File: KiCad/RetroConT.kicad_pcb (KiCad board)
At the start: 2 copper layers, 200 x 200 mm, 213 parts, among them IC1 BH7236, IC2 EPM7128-J84SOC-RetroCon-eagle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, IC21 4464, IC22 4464, IC23 4464, IC24 4464, IC30 74HC157, IC31 74HC157, IC32 74LS07, IC33 74HC14, IC4 74LVC245, IC6 74HC74, IC7 74HC30, J1 POWER, J10 DIN8_SEL2, J11 DIN8_SEL4, J12 RGB, J14 DIN8_SEL1, J17 USB_A_DUAL, J2 SVideo, J4 DIN8_SEL3, J5 MONO, J7 POWER-OUT, J8 DIN8_SEL5, Q2 21M47727, Q4 TP0606N3, Q5 TP0606N3, SW1 SW_SPDT, SW2 SW_SPDT, SW3 SW_DPDT, U1 LM358, U10 RP5C01A, U11 74LS175, U2 Z80/Z84C00, U3 29x010/20/40, U4 AS6C4008, U5 PUD-0512, U6 MDD02L-12, U7 tinyFPGA, U8 LM1117-33, X1 PS/2 KBD, X2 RAUDIO, X3 JOYSTICK1, X4 JOYSTICK2, X5 LAUDIO, X9 COMPOSITE, Y1 32.768KHz

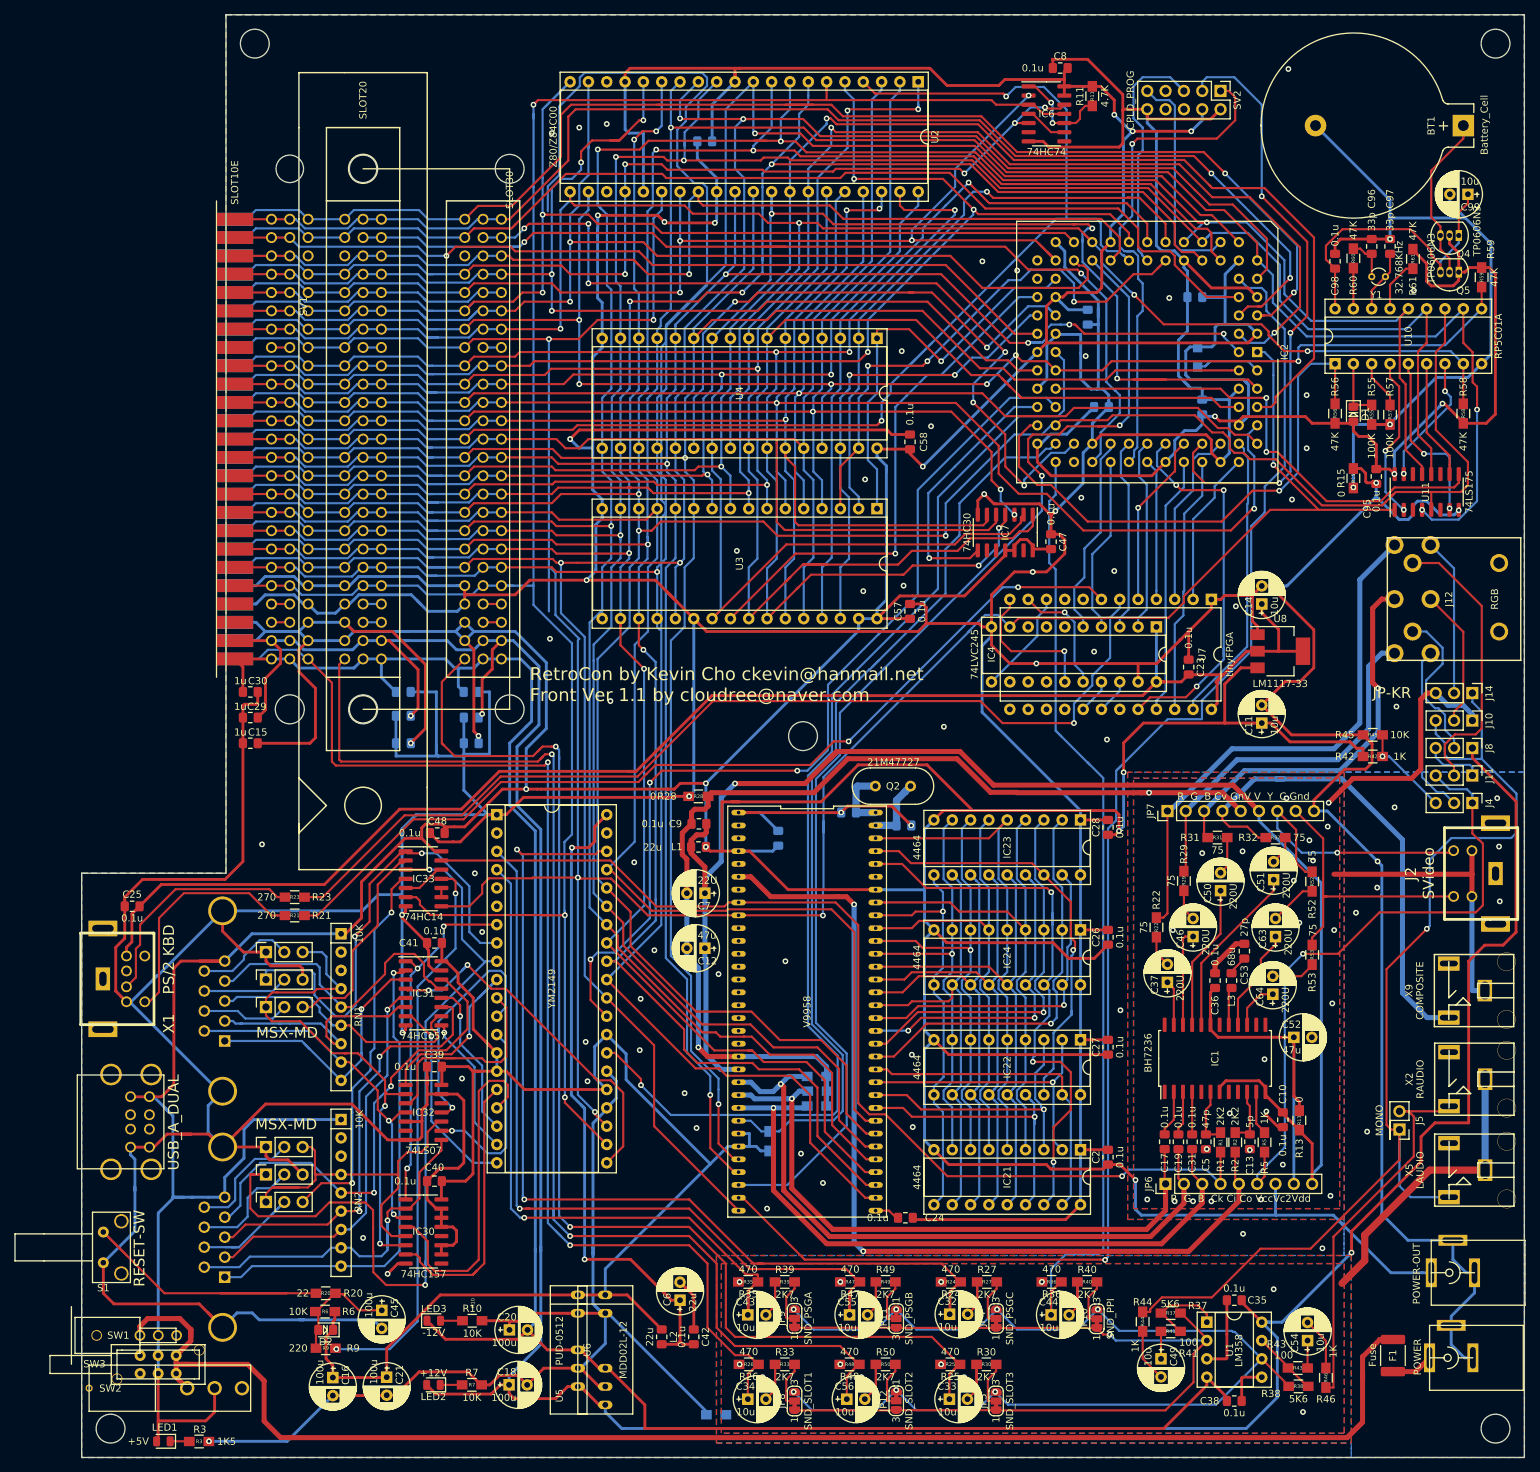
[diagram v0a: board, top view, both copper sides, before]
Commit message: Fix up some bugs
fix up around XTAL and add variable capacitor.
fix the position of Joystick ports.
fix +5V supply around DC2DC.
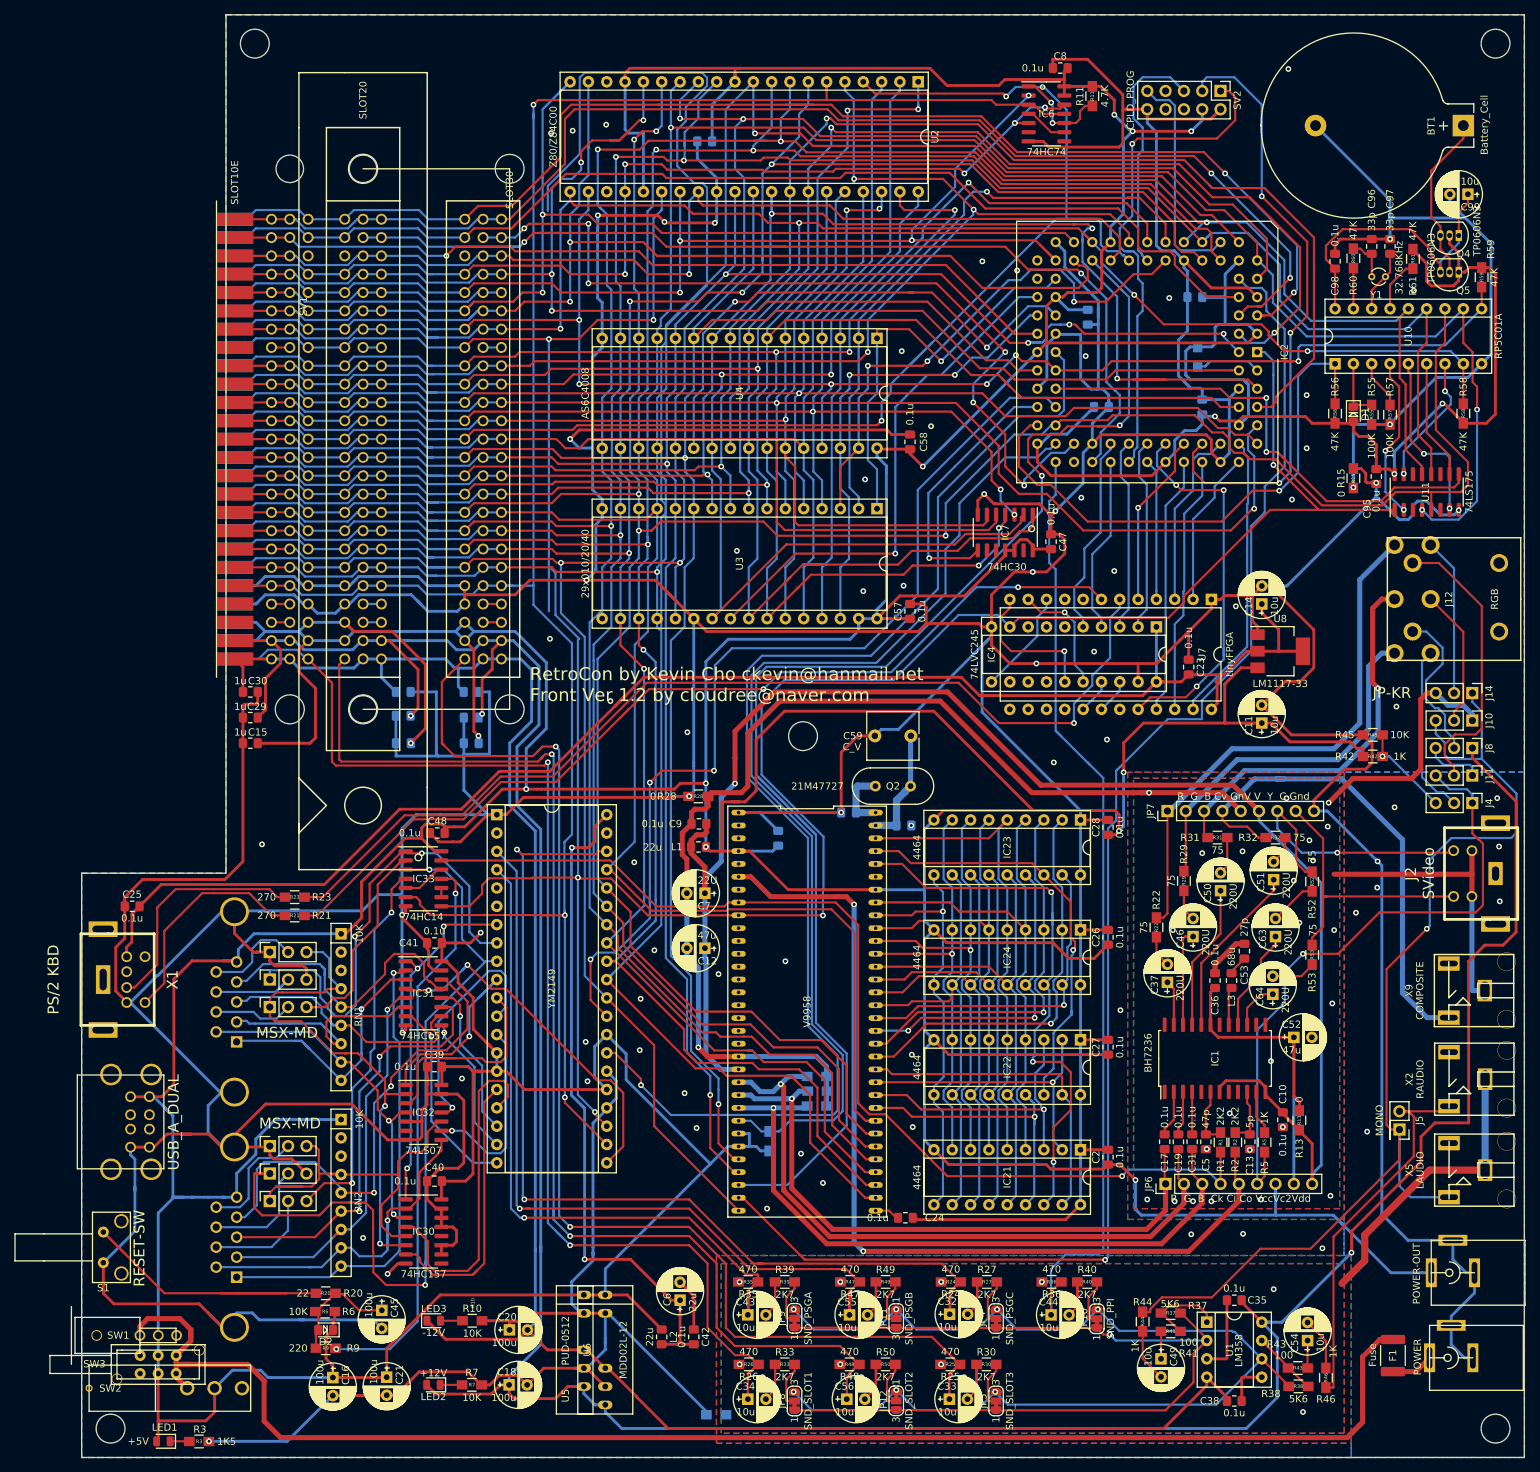
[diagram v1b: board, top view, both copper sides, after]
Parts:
- added C59: C_V, Capacitor_THT:C_Rect_L7.0mm_W6.5mm_P5.00mm, F.Cu at (135.0, 125.0)
- moved X3 1.66 mm to (46.5, 167.4)
- moved X4 1.65 mm to (46.5, 200.0)
- moved U5 0.84 mm to (94.6, 210.1)
- moved JS21 0.55 mm to (51.1, 181.8)
- moved JS22 0.55 mm to (51.1, 185.6)
- moved JS23 0.55 mm to (51.1, 189.5)
- moved JS11 0.53 mm to (51.1, 154.9)
- moved JS12 0.53 mm to (51.1, 158.8)
- moved JS13 0.53 mm to (51.1, 162.6)
- moved X1 0.10 mm to (30.0, 158.8)
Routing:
- net +5V: track 1464.7 -> 1516.2 mm, vias 15 -> 16
- net #VDP_CSW: track 173.1 -> 199.3 mm
- net GND: track 1625.5 -> 1647.5 mm
- net #ExRESET: track 400.1 -> 416.7 mm
- net PSGBDIR: track 161.5 -> 177.4 mm
- net #VDP_INT: track 131.4 -> 143.5 mm
- net VDD_DAC: track 217.7 -> 225.2 mm
- net GNDV: track 234.0 -> 241.5 mm, vias 26 -> 25
- net XTAL1: track 9.16 -> 16.1 mm
- net Q2P7: track 18.7 -> 15.0 mm
- net +3V3: track 208.3 -> 211.7 mm
- net PSGBC1: track 131.4 -> 134.6 mm
- net -12V: track 278.7 -> 276.3 mm
- net J1DN: track 35.6 -> 33.5 mm
- net PSDATA: track 139.0 -> 141.1 mm
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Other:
- board text added: "RetroCon by Kevin Cho ckevin@hanmail.net Front Ver 1.2 by cloudree@naver.com"
- board text removed: "RetroCon by Kevin Cho ckevin@hanmail.net Front Ver 1.1 by cloudree@naver.com"

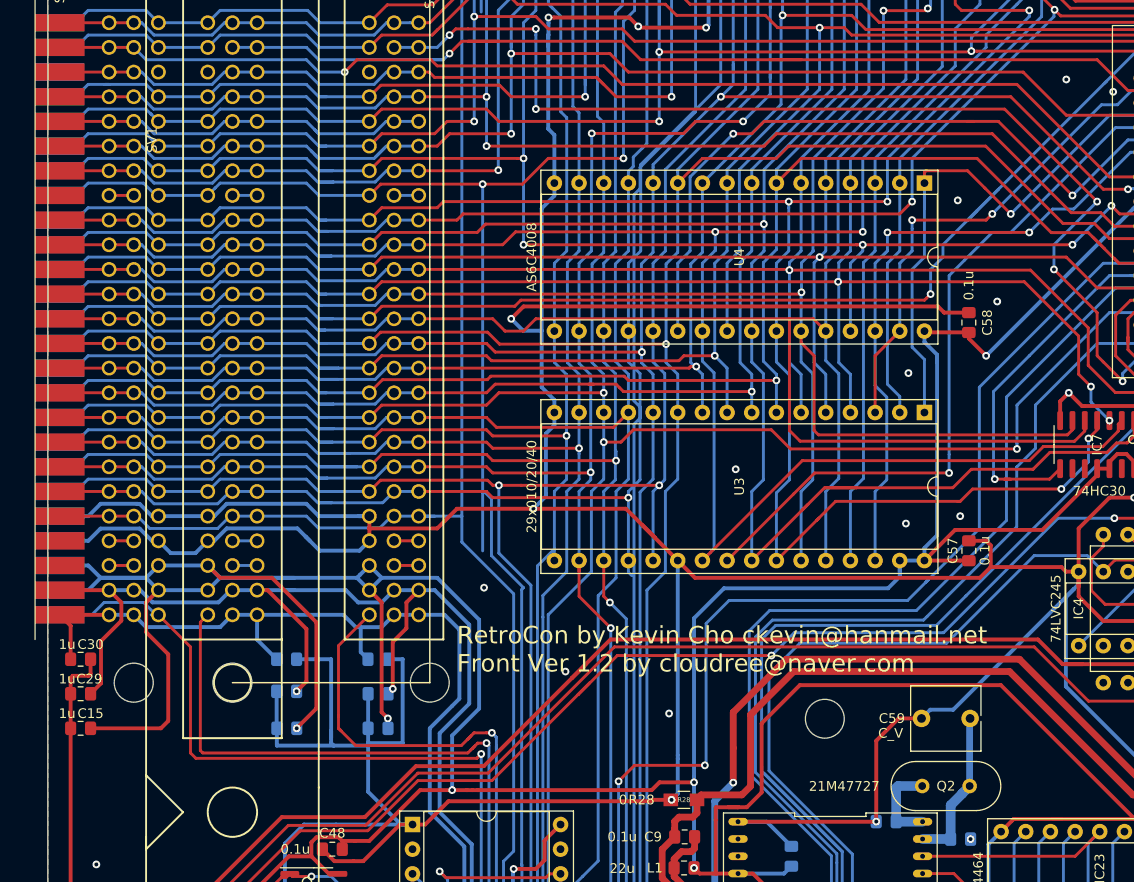
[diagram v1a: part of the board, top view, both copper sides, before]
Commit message: fix up some details
change proper value of Capacitor for XTAL
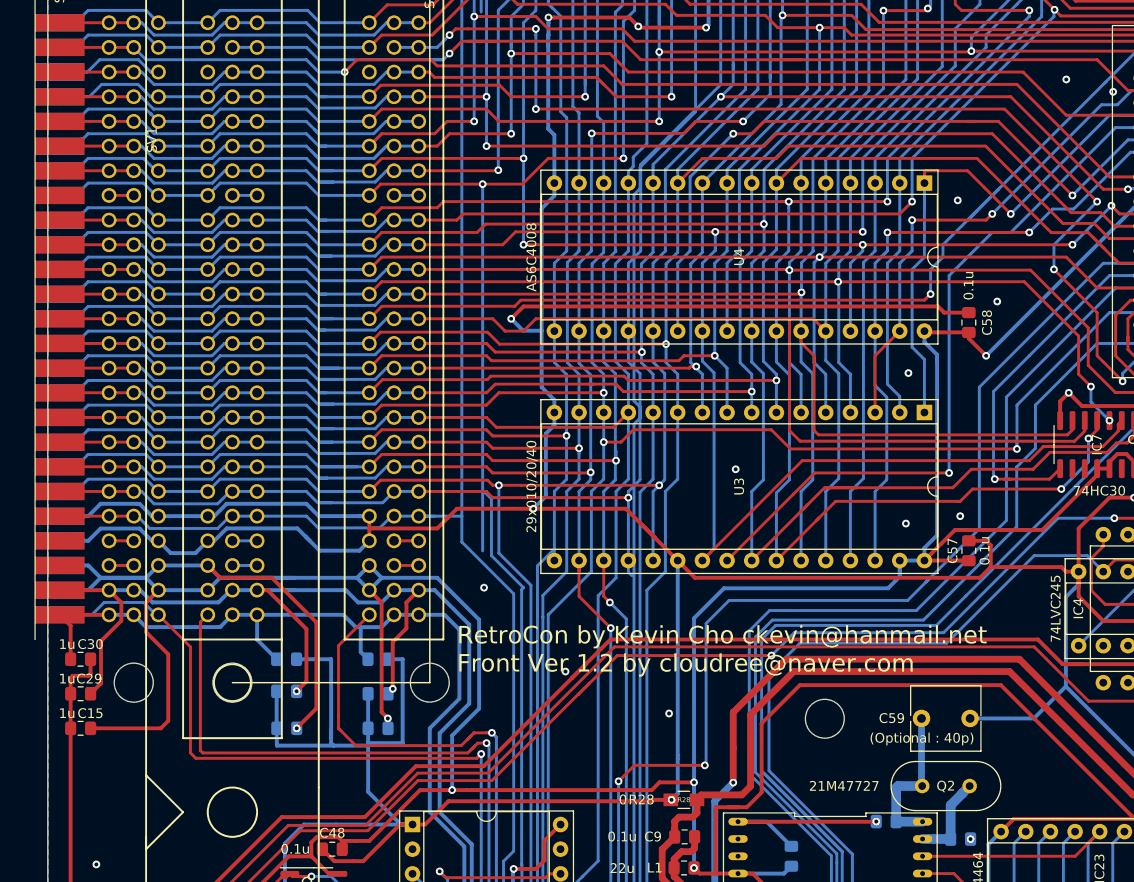
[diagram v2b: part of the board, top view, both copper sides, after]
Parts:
- C22: value 22p -> 47p
- C59: value C_V -> (Optional : 40p)
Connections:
- net Net-(SV1-Pad16) renamed RSV21
- net Net-(SV1-Pad5) renamed RSV20
- net Net-(SV8-Pad16) renamed RSV31
- net Net-(SV8-Pad5) renamed RSV30
- C59 pad 1: GND -> XTAL2
- C59 pad 2: XTAL1 -> GND
- SV3 pad 16: Net-(SV3-Pad16) -> RSV11
- SV3 pad 5: Net-(SV3-Pad5) -> RSV10
- SV4 pad 16: Net-(SV4-Pad16) -> RSV11
- SV4 pad 5: Net-(SV4-Pad5) -> RSV10
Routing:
- net GND: track 1647.5 -> 1623.6 mm
- net RSV10: track 0.00 -> 11.2 mm
- net XTAL2: track 8.96 -> 15.9 mm
- net XTAL1: track 16.1 -> 9.16 mm
- net RSV11: track 0.00 -> 2.54 mm
- net Net-(SV4-Pad16): track 2.54 -> 0.00 mm
